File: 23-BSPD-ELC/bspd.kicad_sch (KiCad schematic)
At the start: 30 parts, among them SW1 TS-1187A-B-A-B, U1 SN74ALS32DR, U2 74HC04D,653, U3 74HC08D,653, U4 74LVC2G17DBVE4, U5 ADM812, U6 CD4043BDR

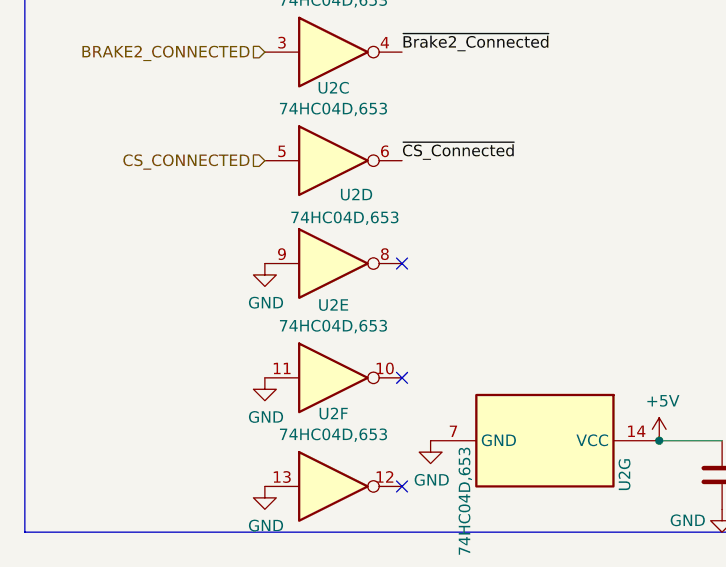
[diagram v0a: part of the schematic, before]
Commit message: Updated connectors and added ~brake signal to vcu
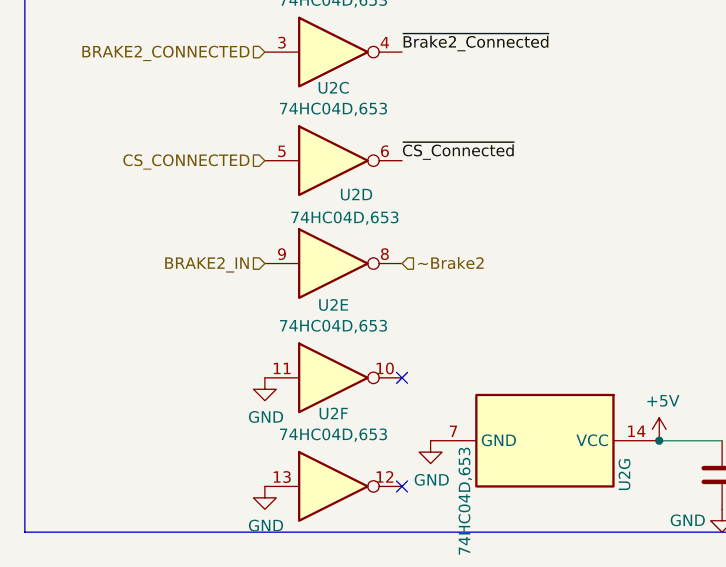
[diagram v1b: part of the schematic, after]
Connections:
- net BRAKE2_IN: now also U2.9
- net GND: no longer U2.9
- net ~Brake2: now reaches U2.8
- no-connect marks 11 -> 10
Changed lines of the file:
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@@
   (no_connect (at 260.35 50.8))
   (no_connect (at 260.35 48.26))
-  (no_connect (at 55.88 166.37))
   (no_connect (at 128.27 115.57))
   (no_connect (at 242.57 33.02))
@@
     (effects (font (size 1.27 1.27)) (justify right))
   )
+  (hierarchical_label "~Brake2" (shape input) (at 55.88 166.37 0)
+    (effects (font (size 1.27 1.27)) (justify left))
+  )
   (hierarchical_label "CS_CONNECTED" (shape input) (at 40.64 154.94 180)
     (effects (font (size 1.27 1.27)) (justify right))
@@
   )
   (hierarchical_label "CS_IN" (shape input) (at 102.87 41.91 180)
+    (effects (font (size 1.27 1.27)) (justify right))
+  )
+  (hierarchical_label "BRAKE2_IN" (shape input) (at 40.64 166.37 180)
     (effects (font (size 1.27 1.27)) (justify right))
   )
@@
       (effects (font (size 1.27 1.27)) hide)
     )
-    (pin "1")
-  )
-  (symbol (lib_id "power:GND") (at 40.64 166.37 0) (unit 1)
-    (in_bom yes) (on_board yes)
-    (property "Reference" "#PWR05" (id 0) (at 40.64 172.72 0)
-      (effects (font (size 1.27 1.27)) hide)
-    )
-    (property "Value" "GND" (id 1) (at 40.767 170.7642 0))
-    (property "Footprint" "" (id 2) (at 40.64 166.37 0)
-      (effects (font (size 1.27 1.27)) hide)
-    )
-    (property "Datasheet" "" (id 3) (at 40.64 166.37 0)
-      (effects (font (size 1.27 1.27)) hide)
-    )

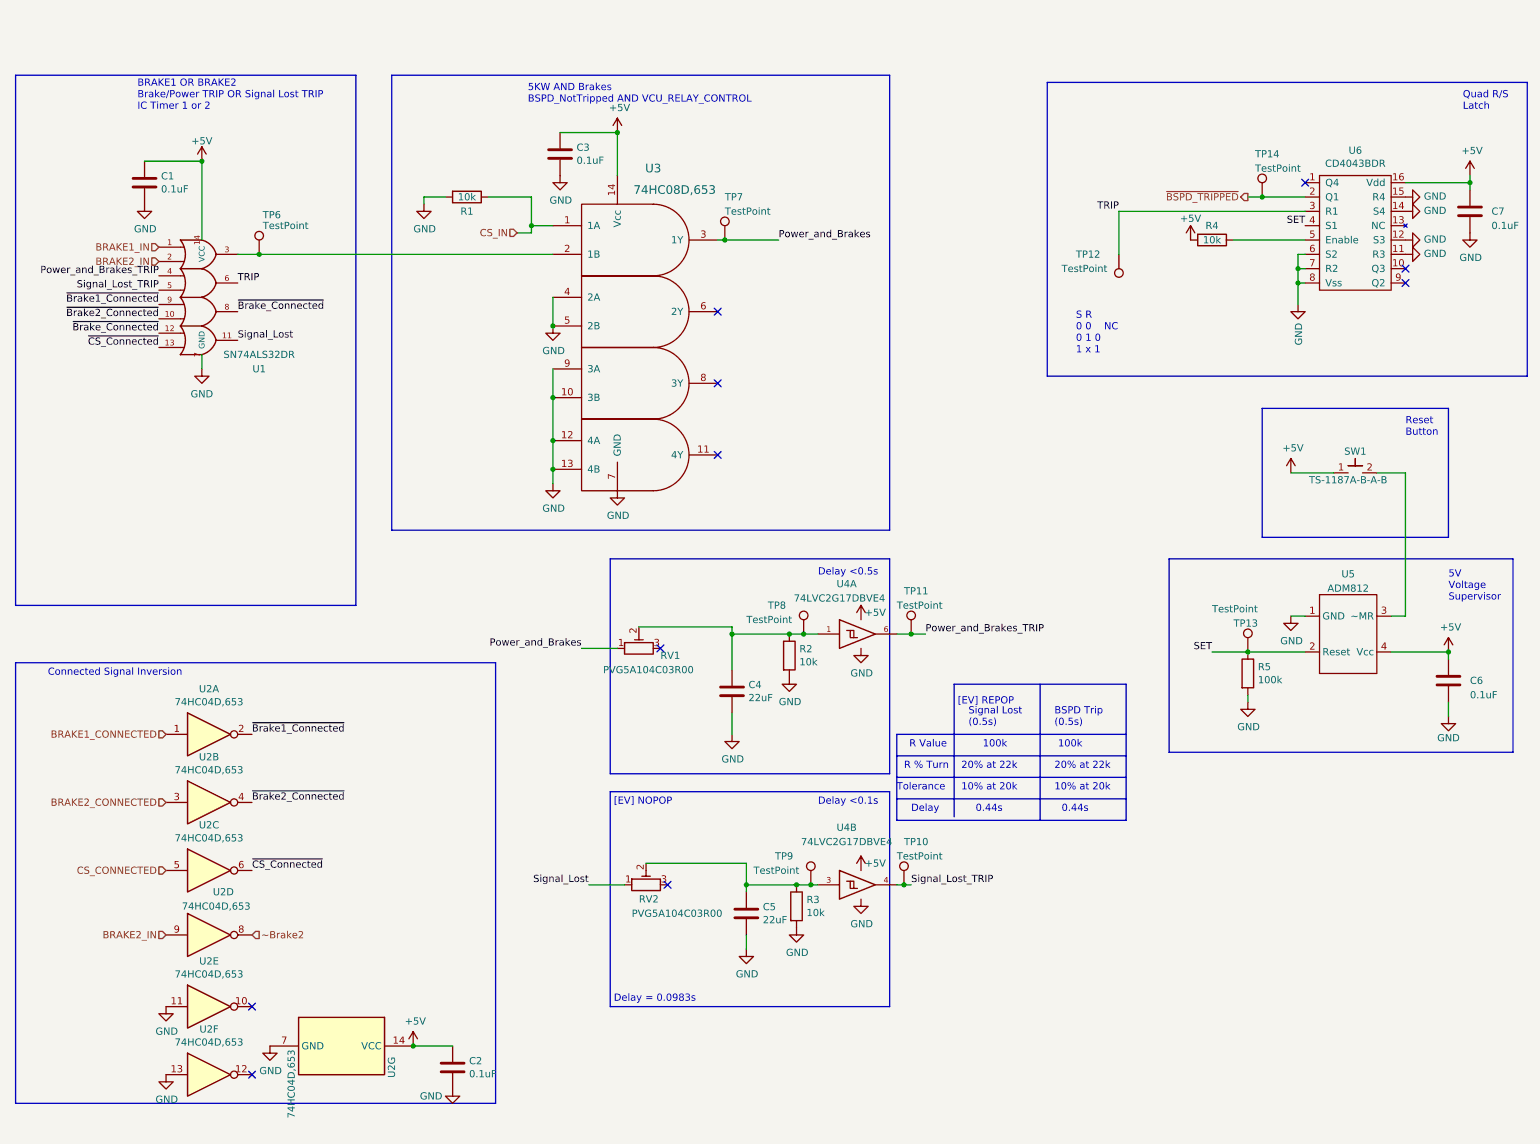
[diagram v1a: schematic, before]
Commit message: Revision changes and updates to some footprints
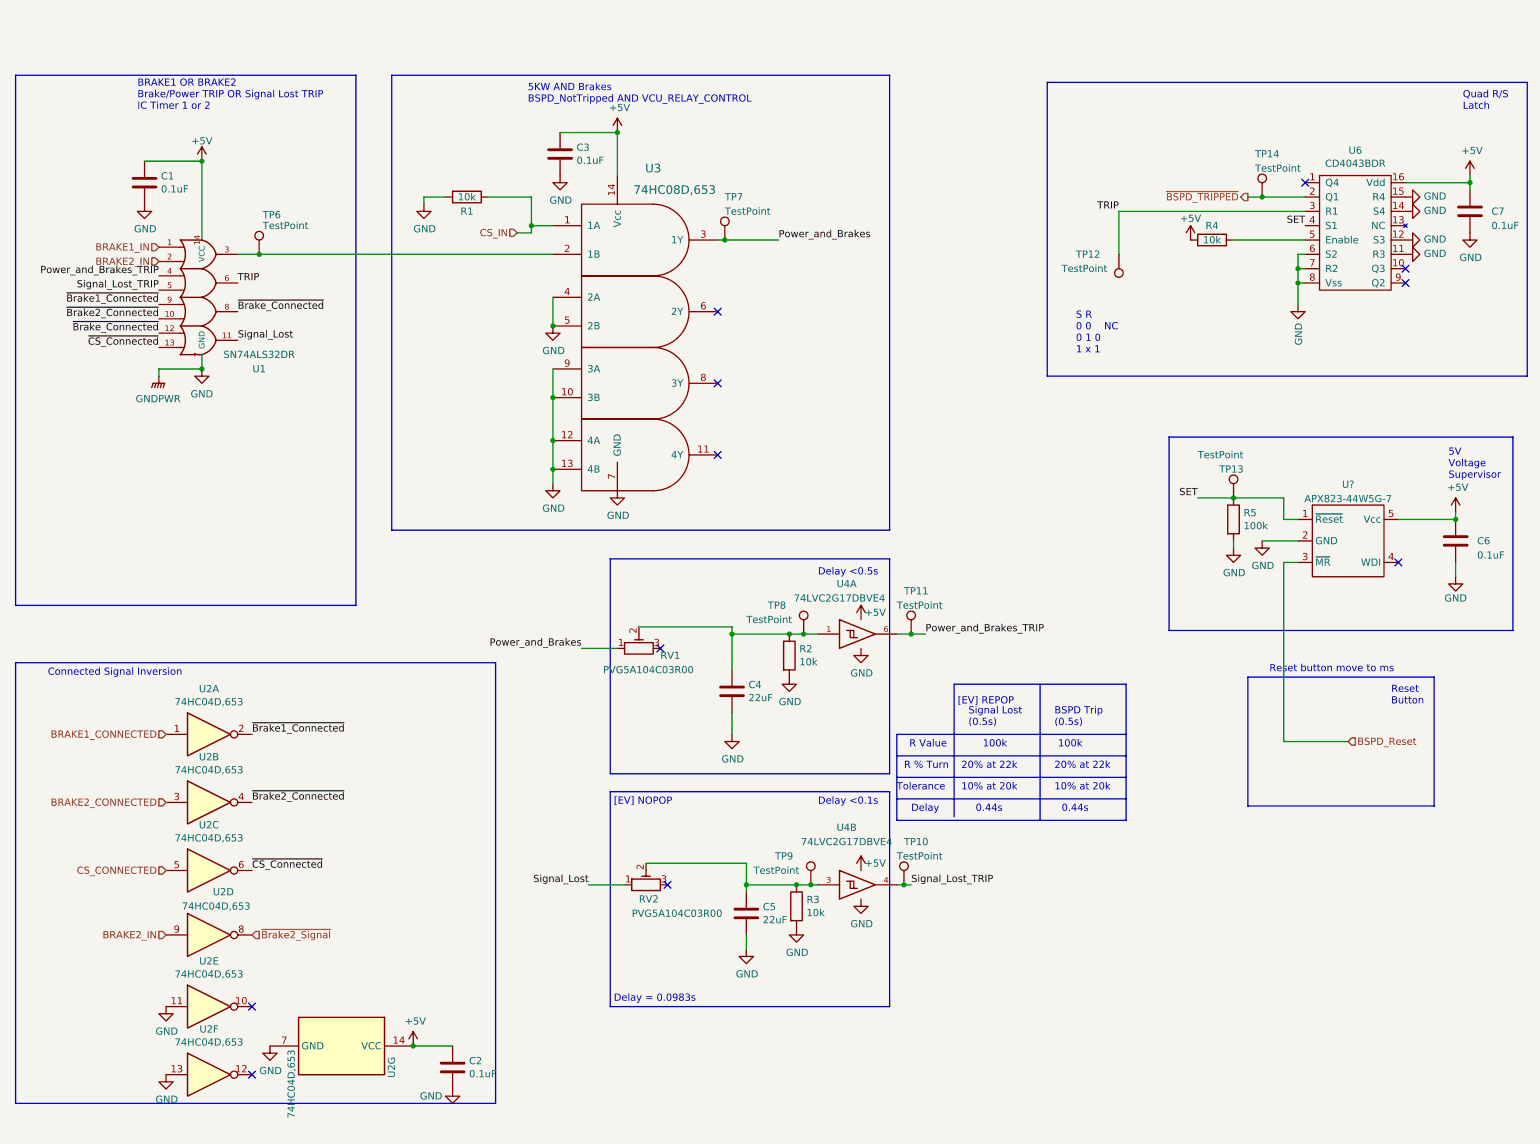
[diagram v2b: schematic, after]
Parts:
- removed SW1: TS-1187A-B-A-B, Button_Switch_SMD:SW_SPST_TL3342, symbol 20-ELC-2-01-R2(Appetizer)-rescue:UK-B0288-SP25Y-LHRE_Component_Library
- removed U5: ADM812, symbol LHR 2023 Schematic Library:ADM812
- added U?: APX823-44W5G-7, symbol Global Library:APX823-44W5G-7
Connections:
- net +5V: now also U?.5 (Vcc)
- net GND: now also U?.2 (GND)
- net SET: now also U?.1 (~{Reset})
- net ~Brake2 renamed ~{Brake2_Signal}
- new net BSPD_Reset: U?.3 (~{MR})
- no-connect marks 10 -> 11
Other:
- note added: "Reset button move to ms"
- moved on the sheet: C6, R5, TP13

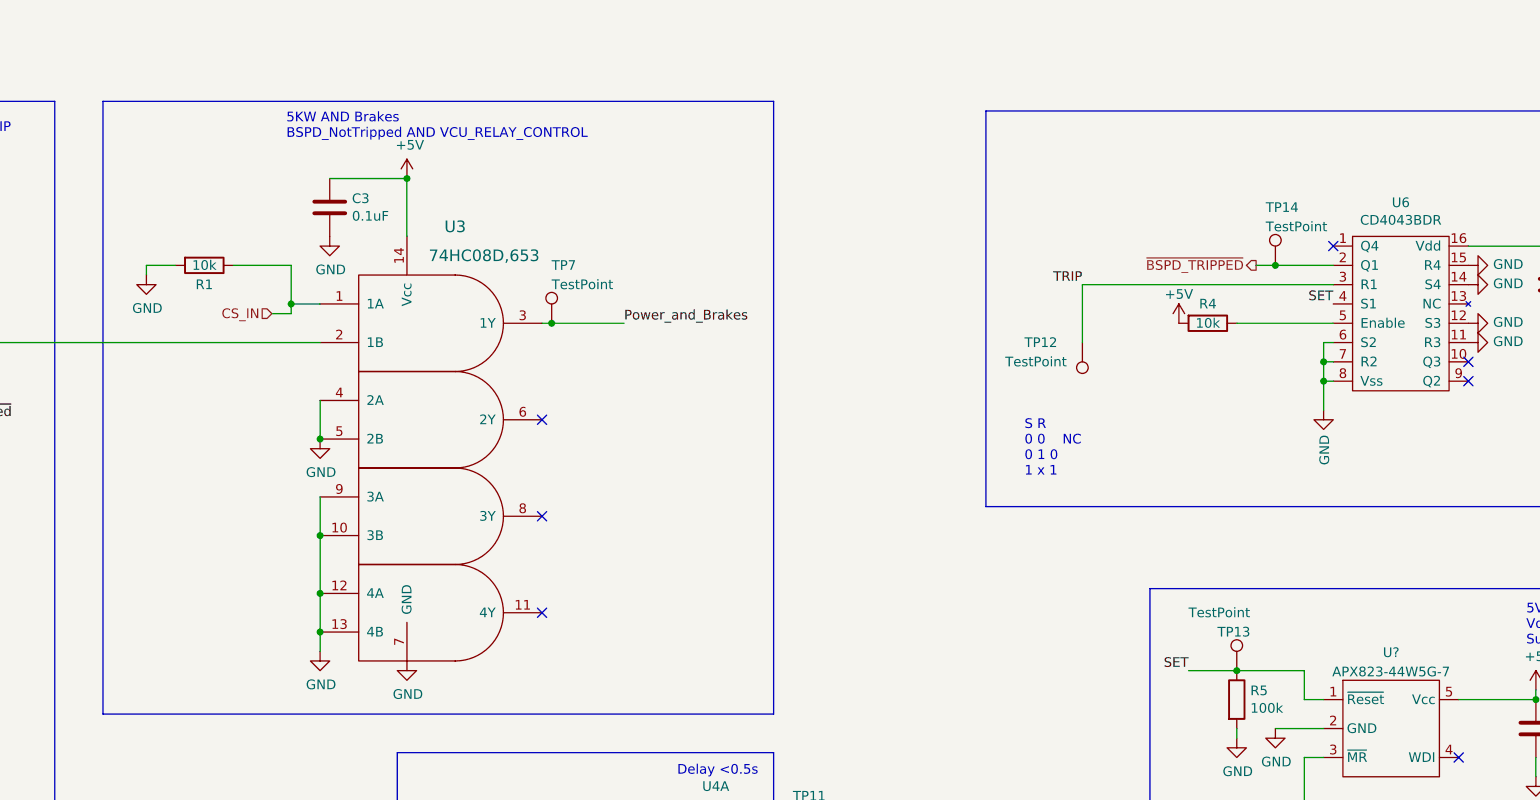
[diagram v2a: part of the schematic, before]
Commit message: Updated pcb layout; Watchdog on board still in progress
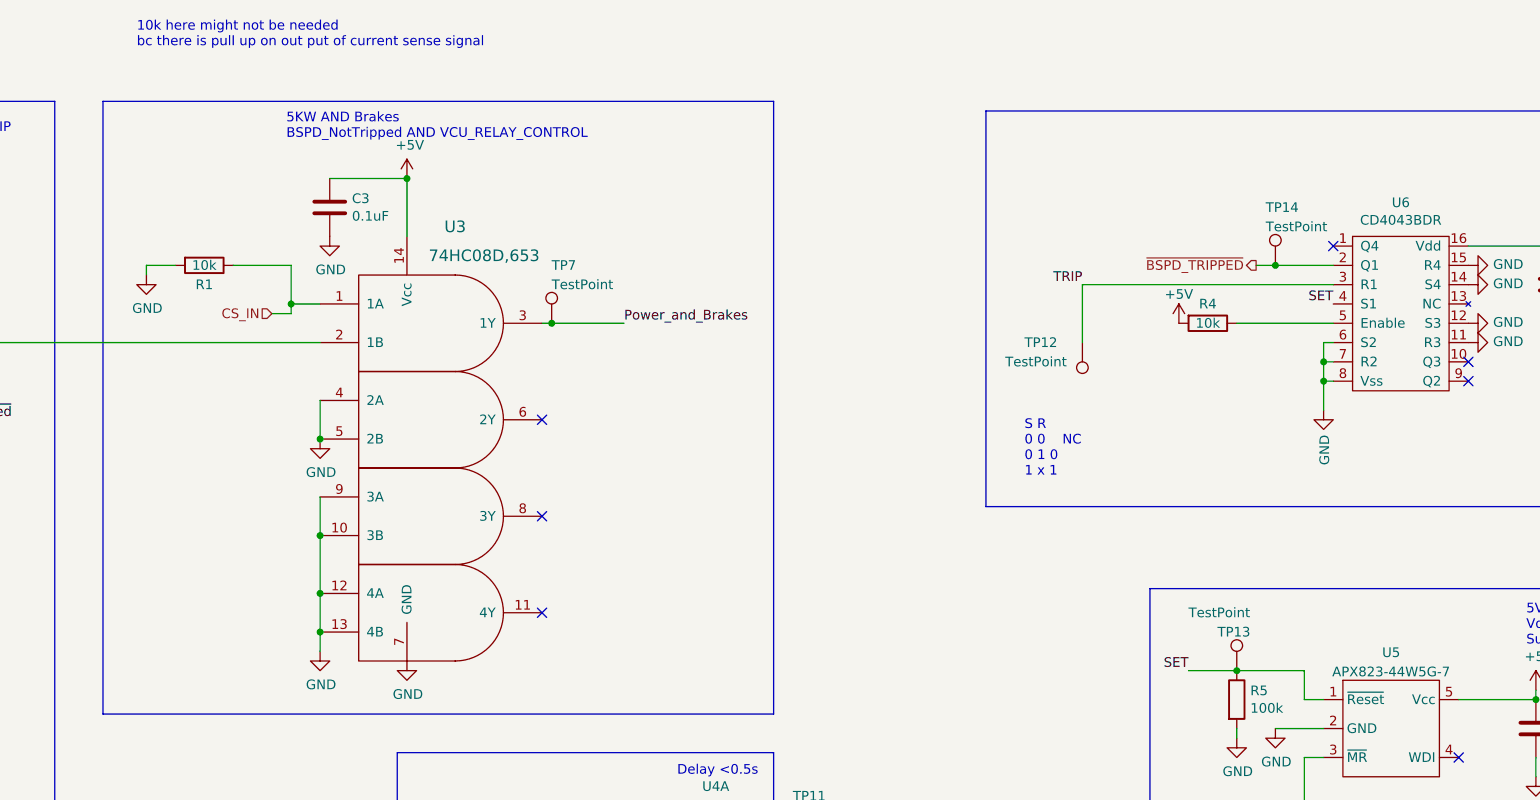
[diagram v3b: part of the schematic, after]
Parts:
- RV1: footprint LHRE Footprint Library:PV36W201C01B00 -> Global Libraries:PVG5A
- RV2: footprint Potentiometer_SMD:Potentiometer_Bourns_3214W_Vertical -> Global Libraries:PVG5A
- U4: footprint LHRE Footprint Library:74LVC2G17 -> Package_TO_SOT_SMD:SOT-23-6
- U5: renamed from U?; footprint (none) -> Global Libraries:AXP823-44W5G-7
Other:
- note added: "10k here might not be needed bc there is pull up on out put of current sense signal"
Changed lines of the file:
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@@
+    (effects (font (size 1.27 1.27)) (justify left bottom))
+  )
+  (text "10k here might not be needed \nbc there is pull up on out put of current sense signal"
+    (at 85.09 6.985 0)
     (effects (font (size 1.27 1.27)) (justify left bottom))
   )
@@
       (effects (font (size 1.27 1.27)) (justify right))
     )
-    (property "Footprint" "LHRE Footprint Library:PV36W201C01B00" (id 2) (at 120.65 124.46 90)
+    (property "Footprint" "Global Libraries:PVG5A" (id 2) (at 120.65 124.46 90)
       (effects (font (size 1.27 1.27)) hide)
     )
@@
       (effects (font (size 1.27 1.27)) (justify right))
     )
-    (property "Footprint" "Potentiometer_SMD:Potentiometer_Bourns_3214W_Vertical" (id 2) (at 125.73 157.48 0)
+    (property "Footprint" "Global Libraries:PVG5A" (id 2) (at 125.73 157.48 0)
       (effects (font (size 1.27 1.27)) hide)
     )
@@
     (property "Reference" "U4" (id 0) (at 161.29 104.14 0))
     (property "Value" "74LVC2G17DBVE4" (id 1) (at 160.02 106.68 0))
-    (property "Footprint" "LHRE Footprint Library:74LVC2G17" (id 2) (at 163.83 113.03 0)
+    (property "Footprint" "Package_TO_SOT_SMD:SOT-23-6" (id 2) (at 163.83 113.03 0)
       (effects (font (size 1.27 1.27)) hide)
     )
@@
     (property "Reference" "U4" (id 0) (at 161.29 147.32 0))
     (property "Value" "74LVC2G17DBVE4" (id 1) (at 161.29 149.86 0))
-    (property "Footprint" "LHRE Footprint Library:74LVC2G17" (id 2) (at 163.83 157.48 0)
+    (property "Footprint" "Package_TO_SOT_SMD:SOT-23-6" (id 2) (at 163.83 157.48 0)
       (effects (font (size 1.27 1.27)) hide)
     )
@@
   (symbol (lib_id "Global Library:APX823-44W5G-7") (at 250.19 96.52 0) (unit 1)
     (in_bom yes) (on_board yes) (fields_autoplaced)
-    (property "Reference" "U?" (id 0) (at 250.19 86.521 0))
+    (property "Reference" "U5" (id 0) (at 250.19 86.521 0))
     (property "Value" "APX823-44W5G-7" (id 1) (at 250.19 89.0579 0))
-    (property "Footprint" "" (id 2) (at 250.19 96.52 0)
-      (effects (font (size 1.27 1.27)) hide)
-    )
+    (property "Footprint" "Global Libraries:AXP823-44W5G-7" (id 2) (at 250.19 96.52 0)
+      (effects (font (size 1.27 1.27)) hide)
+    )
